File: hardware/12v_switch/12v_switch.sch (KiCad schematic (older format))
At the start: 49 parts, among them J1 MOLEX_0530470810, M1 SCREW_6-32_POWER, M11 SCREW_6-32_POWER, M12 SCREW_6-32_POWER, M13 SCREW_6-32_POWER, M14 SCREW_6-32_POWER, M19 SCREW_6-32_NORMAL, M2 SCREW_6-32_POWER, M20 SCREW_6-32_NORMAL, M21 SCREW_6-32_NORMAL, M22 SCREW_6-32_NORMAL, M3 SCREW_6-32_POWER, M4 SCREW_6-32_POWER, M5 SCREW_6-32_POWER, M6 SCREW_6-32_POWER, Q1 INFINEON_IRF7470TRPBF, Q2 INFINEON_IRF7470TRPBF, Q3 INFINEON_IRF7470TRPBF, Q4 INFINEON_IRF7470TRPBF, U1 TI_LM5111-1MX_NOPB, U2 TI_LM5111-1MX_NOPB, U3 TI_LM22680QMRE-ADJ

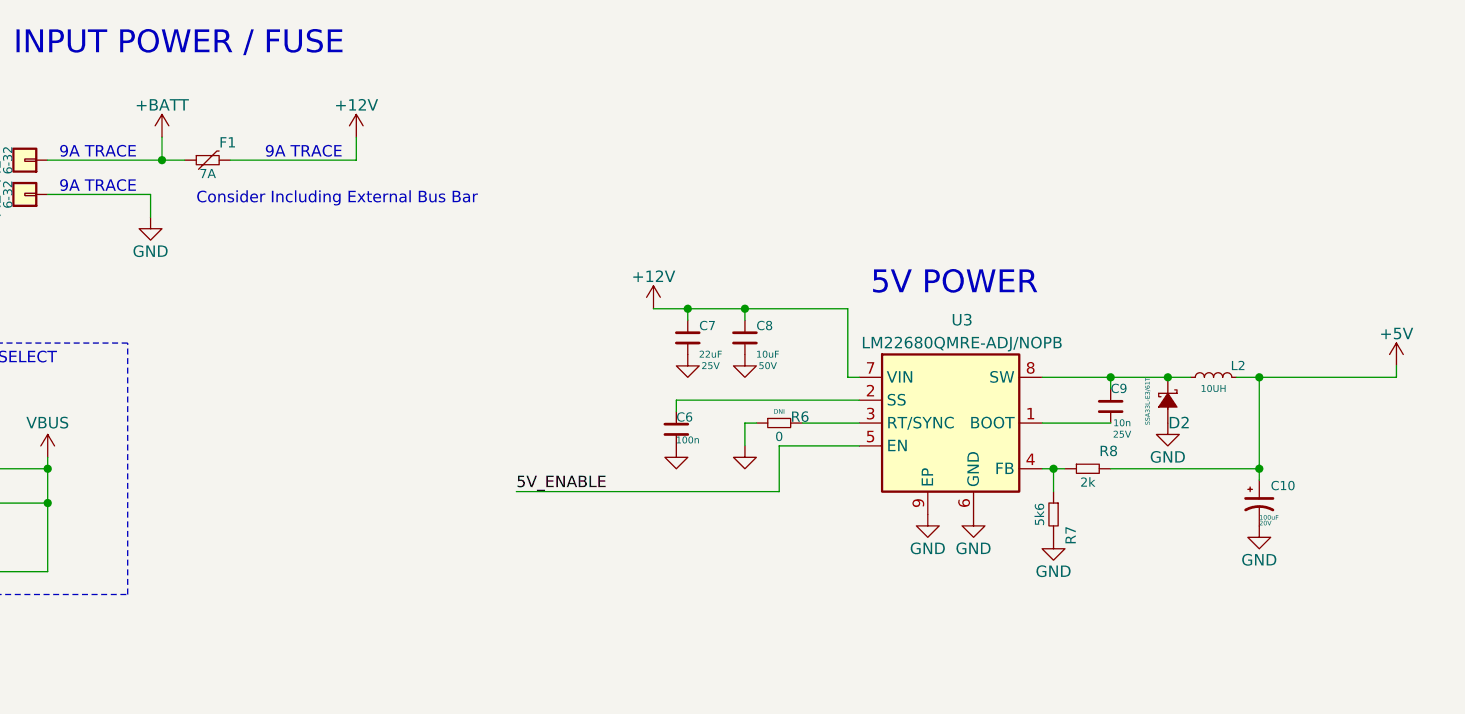
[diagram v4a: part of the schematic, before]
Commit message: added reverse polarity, TVS, and better regulator bypass cap, and fixed feedback resistors
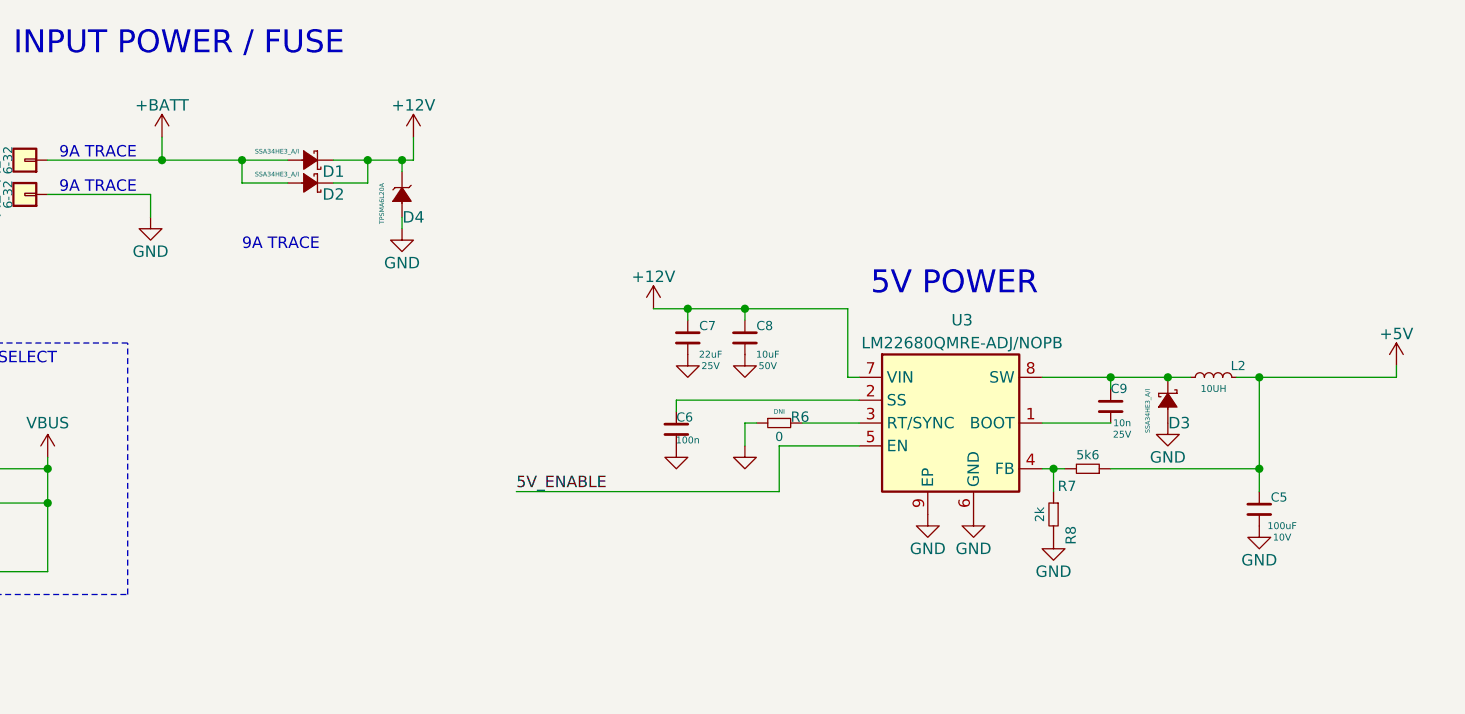
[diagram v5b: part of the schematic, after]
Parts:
- removed C10: VISHAY_593D107X0020E2TE3, DBLS_Capacitor:C_2917, symbol DBLS_Capacitor:VISHAY_593D107X0020E2TE3
- removed D2: VISHAY_SSA33L-E3_61T, Diodes_SMD:D_SMA, symbol DBLS_Diode:VISHAY_SSA33L-E3_61T
- removed F1: LITTLEFUSE_RGEF700-2, DBLS_Misc:LITTLEFUSE_RGEF, symbol DBLS_Misc:LITTLEFUSE_RGEF700-2
- added C5: TAIYO-YUDEN_LMK325ABJ107MM-P, Capacitors_SMD:C_1210, symbol DBLS_Capacitor:TAIYO-YUDEN_LMK325ABJ107MM-P
- added D1, D2, D3: VISHAY_SSA34HE3_A_I, Diodes_SMD:D_SMA, symbol DBLS_Diode:VISHAY_SSA34HE3_A_I
- added D4: LITTLEFUSE_TPSMA6L20A, Diodes_SMD:D_SMA, symbol DBLS_Diode:LITTLEFUSE_TPSMA6L20A
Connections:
- net +12V: now also D1.1 (K), D2.1 (K), D4.1 (K)
- net +5V: now also R7.1, C5.1; no longer R8.2
- net +BATT: now also D1.2 (A), D2.2 (A)
- net GND: now also R8.2, C5.2, D3.2 (A), D4.2 (A); no longer R7.2
- net at C9.1, L2.1, U3.8 (SW): now also D3.1 (K)
- net at R8.1, U3.4 (FB): now also R7.2; no longer R7.1
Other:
- note removed: "Consider Including External Bus Bar\n"
- moved on the sheet: R7, R8
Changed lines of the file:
@@
 Wire Wire Line
 	2350 1450 2350 1350
-Text Notes 2550 1400 0    50   ~ 0
-Consider Including External Bus Bar\n
-Text Notes 2850 1200 0    50   ~ 0
+Text Notes 2750 1600 0    50   ~ 0
 9A TRACE
 Wire Wire Line
-	3250 1200 3250 1100
+	3500 1200 3500 1100
 Text Notes 3050 3850 0    100  ~ 0
 Power Switches
@@
 L power:+12V #PWR0113
 U 1 1 6166E0F4
-P 3250 1100
-F 0 "#PWR0113" H 3250 950 50  0001 C CNN
-F 1 "+12V" H 3250 1240 50  0000 C CNN
-F 2 "" H 3250 1100 50  0001 C CNN
-F 3 "" H 3250 1100 50  0001 C CNN
-	1    3250 1100
+P 3500 1100
+F 0 "#PWR0113" H 3500 950 50  0001 C CNN
+F 1 "+12V" H 3500 1240 50  0000 C CNN
+F 2 "" H 3500 1100 50  0001 C CNN
+F 3 "" H 3500 1100 50  0001 C CNN
+	1    3500 1100
 	1    0    0    -1
 $EndComp
@@
 Wire Wire Line
 	2400 1100 2400 1200
-$Comp
-L DBLS_Misc:LITTLEFUSE_RGEF700-2 F1
-U 1 1 618C02E2
-P 2600 1200
-F 0 "F1" H 2650 1250 45  0000 L BNN
-F 1 "LITTLEFUSE_RGEF700-2" H 2200 1850 50  0001 L BNN
-F 2 "DBLS_Misc:LITTLEFUSE_RGEF" H 2600 1400 50  0001 C CNN
-F 3 "N/A" H 2600 1400 50  0001 C CNN
-F 4 "7A" H 2600 1140 40  0000 C CNN "I_hold"
-F 5 "Littlefuse Inc." H 2600 1800 50  0001 C CNN "mfg"
-F 6 "RGEF700-2" H 2600 1700 50  0001 C CNN "mfg_pn"
-F 7 "Digikey" H 2600 1600 50  0001 C CNN "vendor"
-F 8 "RGEF700-2HFTR-ND" H 2600 1500 50  0001 C CNN "vendor_pn"
-F 9 "YES" H 2500 1250 20  0001 C CNN "place"
-F 10 "PTC RESET FUSE 16V 7A RADIAL" H 2600 1200 50  0001 C CNN "description"
-	1    2600 1200
-	1    0    0    -1
-$EndComp
-Wire Wire Line
-	2500 1200 2400 1200
 Connection ~ 2400 1200
-Wire Wire Line
-	2700 1200 3250 1200
 $Comp
 L power:GND #PWR012
@@
 L DBLS_Resistor:VISHAYDALE_CRCW04022K00JNEDC R8
 U 1 1 618569A8
-P 6450 2550
-F 0 "R8" H 6500 2600 45  0000 L BNN
-F 1 "VISHAYDALE_CRCW04022K00JNEDC" H 6050 3200 50  0001 L BNN
-F 2 "Resistors_SMD:R_0402" H 6450 2750 50  0001 C CNN
-F 3 "N/A" H 6450 2750 50  0001 C CNN
-F 4 "2k" H 6450 2490 40  0000 C CNN "resistance"
-F 5 "Vishay Dale" H 6450 3150 50  0001 C CNN "mfg"
-F 6 "CRCW04022K00JNEDC" H 6450 3050 50  0001 C CNN "mfg_pn"
-F 7 "Digikey" H 6450 2950 50  0001 C CNN "vendor"
-F 8 "541-CRCW04022K00JNEDCTR-ND" H 6450 2850 50  0001 C CNN "vendor_pn"
-F 9 "YES" H 6350 2600 20  0001 C CNN "place"
-	1    6450 2550
-	1    0    0    -1
-$EndComp
-$Comp
-L DBLS_Resistor:VISHAYDALE_CRCW04025K60JNED R7
-U 1 1 618569B4
 P 6300 2750
-F 0 "R7" H 6350 2800 45  0000 L BNN
-F 1 "VISHAYDALE_CRCW04025K60JNED" H 5900 3400 50  0001 L BNN
+F 0 "R8" H 6350 2800 45  0000 L BNN
+F 1 "VISHAYDALE_CRCW04022K00JNEDC" H 5900 3400 50  0001 L BNN
 F 2 "Resistors_SMD:R_0402" H 6300 2950 50  0001 C CNN
 F 3 "N/A" H 6300 2950 50  0001 C CNN
-F 4 "5k6" H 6300 2690 40  0000 C CNN "resistance"
+F 4 "2k" H 6300 2690 40  0000 C CNN "resistance"
 F 5 "Vishay Dale" H 6300 3350 50  0001 C CNN "mfg"
-F 6 "CRCW04025K60JNED" H 6300 3250 50  0001 C CNN "mfg_pn"
+F 6 "CRCW04022K00JNEDC" H 6300 3250 50  0001 C CNN "mfg_pn"
 F 7 "Digikey" H 6300 3150 50  0001 C CNN "vendor"
-F 8 "541-5.6KJTR-ND" H 6300 3050 50  0001 C CNN "vendor_pn"
+F 8 "541-CRCW04022K00JNEDCTR-ND" H 6300 3050 50  0001 C CNN "vendor_pn"
 F 9 "YES" H 6200 2800 20  0001 C CNN "place"
 	1    6300 2750
@@
 $EndComp
 $Comp
-L DBLS_Diode:VISHAY_SSA33L-E3_61T D2
-U 1 1 618569BF
-P 6800 2250
-F 0 "D2" V 6900 2300 50  0000 C CNN
-F 1 "VISHAY_SSA33L-E3_61T" H 6950 2040 50  0001 C CNN
-F 2 "Diodes_SMD:D_SMA" H 6950 2400 50  0001 C CNN
-F 3 "" H 6950 2450 50  0001 C CNN
-F 4 "Vishay General Semiconductor" H 6910 2870 50  0001 C CNN "mfg"
-F 5 "SSA33L-E3/61T" H 6700 2150 20  0000 L BNN "mfg_pn"
-F 6 "Digikey" H 6890 2670 50  0001 C CNN "vendor"
-F 7 "SSA33L-E3/61TGITR-ND" H 6910 2580 50  0001 C CNN "vendor_pn"
-F 8 "YES" H 6700 2200 20  0001 C CNN "PLACE"
-	1    6800 2250
-	0    1    1    0
+L DBLS_Resistor:VISHAYDALE_CRCW04025K60JNED R7
+U 1 1 618569B4
+P 6450 2550
+F 0 "R7" H 6500 2600 45  0000 L BNN
+F 1 "VISHAYDALE_CRCW04025K60JNED" H 6050 3200 50  0001 L BNN
+F 2 "Resistors_SMD:R_0402" H 6450 2750 50  0001 C CNN
+F 3 "N/A" H 6450 2750 50  0001 C CNN
+F 4 "5k6" H 6450 2490 40  0000 C CNN "resistance"
+F 5 "Vishay Dale" H 6450 3150 50  0001 C CNN "mfg"
+F 6 "CRCW04025K60JNED" H 6450 3050 50  0001 C CNN "mfg_pn"
+F 7 "Digikey" H 6450 2950 50  0001 C CNN "vendor"
+F 8 "541-5.6KJTR-ND" H 6450 2850 50  0001 C CNN "vendor_pn"
+F 9 "YES" H 6350 2600 20  0001 C CNN "place"
+	1    6450 2550
+	-1   0    0    1
 $EndComp
 $Comp
@@
 	1    0    0    -1
 $EndComp
-Wire Wire Line
-	6800 2150 6550 2150
 Wire Wire Line
 	7100 2150 7200 2150
@@
 	4950 2350 5000 2350
 Wire Wire Line
-	7200 2600 7200 2550
+	7200 2650 7200 2550
 Connection ~ 7200 2550
 $Comp
@@
 	1    0    0    -1
 $EndComp
-Connection ~ 6800 2150
-Wire Wire Line
-	6800 2150 6900 2150
 $Comp
 L DBLS_Inductor:PANASONIC_ETQ-P3M100KVN L2
@@
 F 10 "FIXED IND 33UH 3A 60 MOHM SMD" H 7050 2205 30  0001 C CNN "Description"
 	1    7000 2150
-	1    0    0    -1
-$EndComp
-$Comp
-L DBLS_Capacitor:VISHAY_593D107X0020E2TE3 C10
-U 1 1 61856A0E
-P 7200 2700
-F 0 "C10" H 7250 2775 40  0000 L CNN
-F 1 "VISHAY_593D107X0020E2TE3" H 6750 3550 50  0001 L CNN
-F 2 "DBLS_Capacitor:C_2917" H 7200 3050 50  0001 C CNN
-F 3 "" H 7200 2925 20  0001 C CNN
-F 4 "100uF" H 7200 2625 20  0000 L BNN "capacitance"
-F 5 "Vishay Sprague" H 7200 3450 50  0001 C CNN "mfg"
-F 6 "593D107X0020E2TE3" H 7200 3350 50  0001 C CNN "mfg_pn"
-F 7 "Digikey" H 7200 3250 50  0001 C CNN "vendor"
-F 8 "718-1970-2-ND" H 7200 3150 50  0001 C CNN "vendor_pn"
-F 9 "YES" H 7125 2775 20  0001 C CNN "place"
-F 10 "20V" H 7200 2600 20  0000 L BNN "voltage"
-	1    7200 2700
 	1    0    0    -1
 $EndComp
@@
 	1    0    0    -1
 $EndComp
+Wire Wire Line
+	6550 2150 6800 2150
+$Comp
+L DBLS_Diode:VISHAY_SSA34HE3_A_I D3
+U 1 1 618026C5
+P 6800 2250
+F 0 "D3" V 6900 2300 50  0000 C CNN
+F 1 "VISHAY_SSA34HE3_A_I" H 6950 2040 50  0001 C CNN
+F 2 "Diodes_SMD:D_SMA" H 6950 2400 50  0001 C CNN
+F 3 "" H 6950 2450 50  0001 C CNN
+F 4 "Vishay General Semiconductor" H 6910 2870 50  0001 C CNN "mfg"
+F 5 "SSA34HE3_A/I" H 6750 2150 20  0000 L BNN "mfg_pn"
+F 6 "Digikey" H 6890 2670 50  0001 C CNN "vendor"
+F 7 "SSA34HE3_A/IGITR-ND" H 6910 2580 50  0001 C CNN "vendor_pn"
+F 8 "YES" H 6700 2200 20  0001 C CNN "PLACE"
+	1    6800 2250
+	0    1    1    0
+$EndComp
+Connection ~ 6800 2150
+Wire Wire Line
+	6800 2150 6900 2150
+$Comp
+L DBLS_Diode:VISHAY_SSA34HE3_A_I D1
+U 1 1 618045C1
+P 3050 1200
+F 0 "D1" H 2950 1250 50  0000 C CNN
+F 1 "VISHAY_SSA34HE3_A_I" H 3200 990 50  0001 C CNN
+F 2 "Diodes_SMD:D_SMA" H 3200 1350 50  0001 C CNN
+F 3 "" H 3200 1400 50  0001 C CNN
+F 4 "Vishay General Semiconductor" H 3160 1820 50  0001 C CNN "mfg"
+F 5 "SSA34HE3_A/I" H 3100 1150 20  0000 L BNN "mfg_pn"
+F 6 "Digikey" H 3140 1620 50  0001 C CNN "vendor"
+F 7 "SSA34HE3_A/IGITR-ND" H 3160 1530 50  0001 C CNN "vendor_pn"
+F 8 "YES" H 2950 1150 20  0001 C CNN "PLACE"
+	1    3050 1200
+	-1   0    0    1
+$EndComp
+Wire Wire Line
+	3150 1200 3300 1200
+$Comp
+L DBLS_Diode:VISHAY_SSA34HE3_A_I D2
+U 1 1 6180E936
+P 3050 1300
+F 0 "D2" H 2950 1350 50  0000 C CNN
+F 1 "VISHAY_SSA34HE3_A_I" H 3200 1090 50  0001 C CNN
+F 2 "Diodes_SMD:D_SMA" H 3200 1450 50  0001 C CNN
+F 3 "" H 3200 1500 50  0001 C CNN
+F 4 "Vishay General Semiconductor" H 3160 1920 50  0001 C CNN "mfg"
+F 5 "SSA34HE3_A/I" H 3100 1250 20  0000 L BNN "mfg_pn"
+F 6 "Digikey" H 3140 1720 50  0001 C CNN "vendor"
+F 7 "SSA34HE3_A/IGITR-ND" H 3160 1630 50  0001 C CNN "vendor_pn"
+F 8 "YES" H 2950 1250 20  0001 C CNN "PLACE"
+	1    3050 1300
+	-1   0    0    1
+$EndComp
+Wire Wire Line
+	2950 1300 2750 1300
+Wire Wire Line
+	2750 1300 2750 1200
+Connection ~ 2750 1200
+Wire Wire Line
+	2750 1200 2950 1200
+Wire Wire Line
+	3150 1300 3300 1300
+Wire Wire Line
+	3300 1300 3300 1200
+Connection ~ 3300 1200
+Wire Wire Line
+	3300 1200 3450 1200
+Wire Wire Line
+	2400 1200 2750 1200
+$Comp
+L DBLS_Diode:LITTLEFUSE_TPSMA6L20A D4
+U 1 1 61861944
+P 3450 1350
+F 0 "D4" V 3550 1400 50  0000 C CNN
+F 1 "LITTLEFUSE_TPSMA6L20A" H 3600 1140 50  0001 C CNN
+F 2 "Diodes_SMD:D_SMA" H 3600 1500 50  0001 C CNN
+F 3 "" H 3600 1550 50  0001 C CNN
+F 4 "Littlefuse Inc." H 3560 1970 50  0001 C CNN "mfg"
+F 5 "TPSMA6L20A" H 3400 1250 20  0000 L BNN "mfg_pn"
+F 6 "Digikey" H 3540 1770 50  0001 C CNN "vendor"
+F 7 "F6157TR-ND" H 3560 1680 50  0001 C CNN "vendor_pn"
+F 8 "YES" H 3350 1300 20  0001 C CNN "PLACE"
+	1    3450 1350
+	0    1    1    0
+$EndComp
+Wire Wire Line
+	3450 1250 3450 1200
+Connection ~ 3450 1200
+Wire Wire Line
+	3450 1200 3500 1200
+$Comp
+L power:GND #PWR03
+U 1 1 61867435
+P 3450 1500
+F 0 "#PWR03" H 3450 1250 50  0001 C CNN
+F 1 "GND" H 3450 1350 50  0000 C CNN
+F 2 "" H 3450 1500 50  0001 C CNN
+F 3 "" H 3450 1500 50  0001 C CNN
+	1    3450 1500
+	1    0    0    -1
+$EndComp
+Wire Wire Line
+	3450 1500 3450 1450
+$Comp
+L DBLS_Capacitor:TAIYO-YUDEN_LMK325ABJ107MM-P C5
+U 1 1 618D0DDC
+P 7200 2750
+F 0 "C5" H 7250 2825 40  0000 L CNN
+F 1 "TAIYO-YUDEN_LMK325ABJ107MM-P" H 6750 3600 50  0001 L CNN
+F 2 "Capacitors_SMD:C_1210" H 7200 3100 50  0001 C CNN
+F 3 "" H 7200 2975 20  0001 C CNN
+F 4 "100uF" H 7300 2700 30  0000 C CNN "capacitance"
+F 5 "Taiyo Yuden" H 7200 3500 50  0001 C CNN "mfg"
+F 6 "LMK325ABJ107MM-P" H 7200 3400 50  0001 C CNN "mfg_pn"
+F 7 "Digikey" H 7200 3300 50  0001 C CNN "vendor"
+F 8 "587-4317-2-ND" H 7200 3200 50  0001 C CNN "vendor_pn"
+F 9 "YES" H 7125 2825 20  0001 C CNN "place"
+F 10 "10V" H 7300 2650 30  0000 C CNN "voltage"
+F 11 "CAP CER 100UF 10V X5R 1210" H 7200 2750 50  0001 C CNN "description"
+	1    7200 2750
+	1    0    0    -1
+$EndComp
